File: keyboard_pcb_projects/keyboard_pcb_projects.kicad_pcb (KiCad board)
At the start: 2 copper layers, 157 parts, among them J1 AVR-ISP-6, SW1 SW_Push_Reset, SW10 8, SW11 9, SW12 0, SW13 -, SW14 =, SW15 Backspace, SW16 Page Up, SW17 Tab, SW18 Q, SW19 W, SW20 E, SW21 R, SW22 T, SW23 Y, SW24 U, SW25 I, SW26 O, SW27 P, SW28 [, SW29 ], SW3 1, SW30 \, SW31 Page Dn, SW32 Caps Lock, SW33 A, SW34 S, SW35 D, SW36 F, SW37 G, SW38 H, SW39 J, SW4 2, SW40 K, SW41 L, SW42 ;, SW43 ', SW44 Enter, SW46 Insert, SW47 Shift Left, SW48 Z, SW49 X, SW5 3, SW50 C, SW51 V, SW52 B, SW53 N, SW54 M, SW55 ,, SW56 ., SW57 /, SW58 Shift Right, SW6 4, SW60 Up, SW61 Delete, SW62 Ctrl, SW63 Win, SW64 Alt, SW65 Space, SW66 Alt, SW67 Fn, SW68 Left, SW69 Down, SW7 5, SW70 Right, SW71 Ctrl, SW8 6, SW9 7, U1 ATmega32U4-A, Y1 Crystal_GND24_Small

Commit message: More wiring progress
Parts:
- moved D1 4.88 mm to (194.1, 79.2)
- moved C2 3.96 mm to (234.2, 177.0)
- moved C3 3.87 mm to (234.2, 174.0)
- moved C4 3.31 mm to (227.2, 169.0)
- moved F1 2.61 mm to (189.0, 83.0)
- moved Y1 2.43 mm to (228.7, 175.4), turned to 90 degrees
- moved R6 1.18 mm to (199.0, 76.0)
- moved R5 1.06 mm to (189.0, 76.0)
- moved C1 1.03 mm to (218.5, 166.5)
- moved USB1 0.47 mm to (194.0, 63.7)
- turned C6 to 90 degrees
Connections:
- C5 pad 1: Net-(C5-Pad1) -> +5V
- C6 pad 1: Net-(C5-Pad1) -> +5V
- C7 pad 1: Net-(C5-Pad1) -> +5V
- C8 pad 1: Net-(C5-Pad1) -> +5V
- R5 pad 1: Net-(USB1-CC2) -> Net-(USB1-CC1)
- R6 pad 1: Net-(USB1-CC1) -> Net-(USB1-CC2)
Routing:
- net row4: track 0.00 -> 288.1 mm
- net row0: track 0.00 -> 285.8 mm
- net row1: track 0.00 -> 281.0 mm
- net row2: track 0.00 -> 278.6 mm
- net row3: track 0.00 -> 273.8 mm
- net GND: track 0.00 -> 220.0 mm, vias 0 -> 9
- net +5V: track 0.00 -> 204.8 mm, vias 0 -> 7
- net /USB_D_N: track 0.00 -> 104.9 mm, vias 0 -> 2
- net /USB_D_P: track 5.45 -> 108.1 mm, vias 0 -> 2
- net col14: track 0.00 -> 77.7 mm, vias 0 -> 5
- net VCC: track 0.00 -> 24.8 mm, vias 0 -> 2
- net Net-(D71-A): track 0.00 -> 16.0 mm
- net Net-(D69-A): track 0.00 -> 16.0 mm
- net Net-(D68-A): track 0.00 -> 16.0 mm
- net Net-(D66-A): track 0.00 -> 16.0 mm
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- added copper zone on B.Cu, net GND
- added copper zone on F.Cu, net GND
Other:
- board outline added: 332 x 137.5 mm

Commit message: synchronizing between OS workspaces
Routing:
- net col0: track 85.6 -> 258.6 mm, vias 5 -> 9
- net col14: track 77.7 -> 232.6 mm, vias 5 -> 7
- net col1: track 95.4 -> 244.9 mm, vias 5 -> 9
- net col13: track 80.7 -> 216.3 mm, vias 4 -> 8
- net col2: track 93.1 -> 219.6 mm, vias 5 -> 9
- net col12: track 90.0 -> 203.6 mm, vias 4 -> 8
- net row1: track 281.0 -> 384.9 mm, vias 0 -> 2
- net col3: track 91.0 -> 190.7 mm, vias 5 -> 9
- net col4: track 67.0 -> 156.5 mm, vias 4 -> 10
- net row0: track 285.8 -> 373.3 mm, vias 0 -> 9
- net +5V: track 204.8 -> 285.3 mm, vias 7 -> 6
- net col11: track 97.4 -> 175.8 mm, vias 5 -> 6
- net RESET: track 0.00 -> 73.3 mm, vias 0 -> 7
- net col9: track 67.0 -> 133.1 mm, vias 4 -> 8
- net col10: track 88.5 -> 151.2 mm, vias 5 -> 8
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
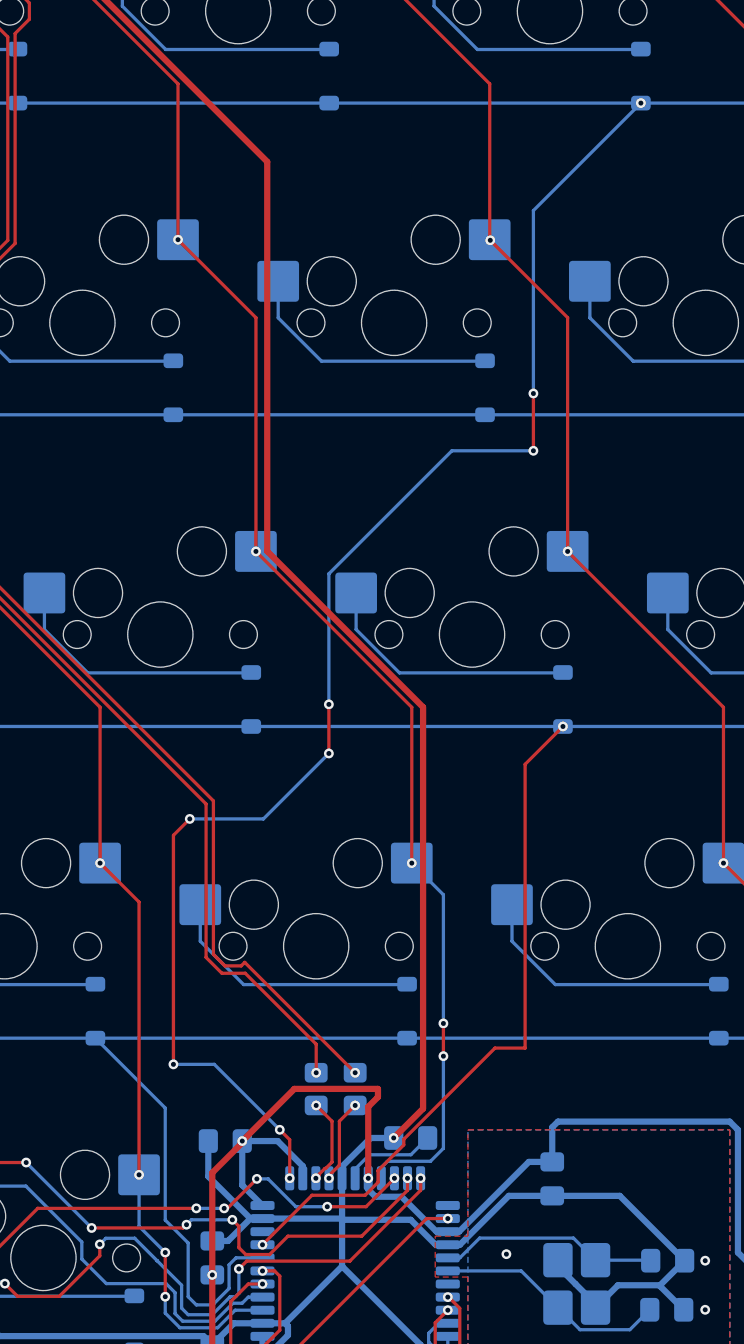
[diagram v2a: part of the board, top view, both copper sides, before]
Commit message: finally cleared all errors but the inherent usbc port sizing issue
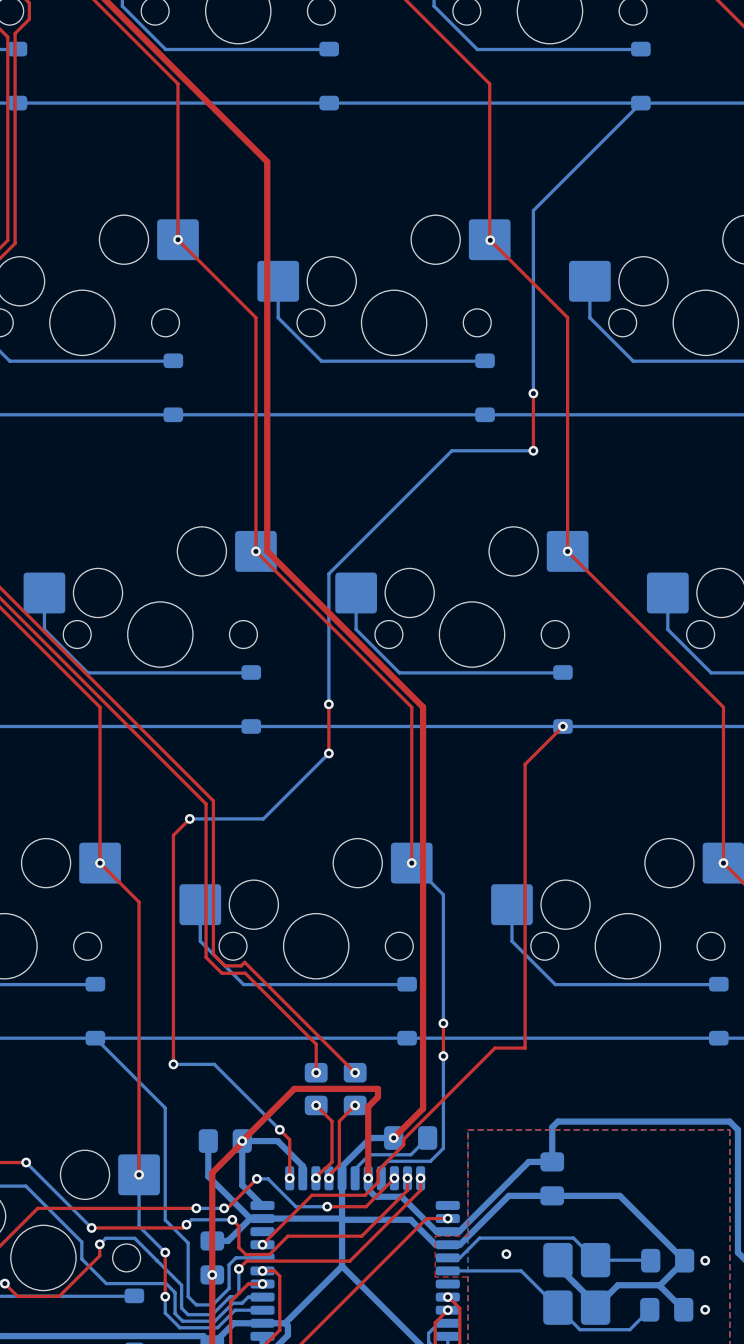
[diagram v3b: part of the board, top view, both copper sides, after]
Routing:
- net row0: vias 9 -> 8
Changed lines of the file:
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@@
 		(tags "capacitor handsolder")
 		(property "Reference" "C5"
-			(at 0 1.68 90)
+			(at 4.33125 -1.375 90)
 			(layer "B.SilkS")
 			(effects
@@
 		(tags "resistor handsolder")
 		(property "Reference" "R4"
-			(at 0 1.65 90)
+			(at -2.0125 4.60625 180)
 			(layer "B.SilkS")
 			(effects
@@
 		(tags "capacitor handsolder")
 		(property "Reference" "C3"
-			(at 0 1.68 0)
+			(at 2.79375 1.68 0)
 			(layer "B.SilkS")
 			(effects
@@
 		(tags "TQFP QFP Microchip_44-Lead-Plastic-Thin-Quad-Flatpack-(PT)")
 		(property "Reference" "U1"
-			(at 0 7.35 90)
+			(at 0.375 3.60625 90)
 			(layer "B.SilkS")
 			(effects
@@
 	(segment
 		(start 201.633679 172.63035)
-		(end 201.63035 172.63035)
+		(end 199.86965 172.63035)
 		(width 0.2)
 		(layer "B.Cu")
@@
 	)
 	(segment
-		(start 207.46863 176.2)
-		(end 206.368628 177.3)
+		(start 203.003329 174)
+		(end 203 174)
 		(width 0.2)
 		(layer "B.Cu")
@@
 	)
 	(segment
-		(start 206.368628 177.3)
-		(end 204.9 177.3)
+		(start 204.5 176.9)
+		(end 204.5 175.496671)
 		(width 0.2)
 		(layer "B.Cu")
@@
 	)
 	(segment
-		(start 208 176.000001)
-		(end 207.800001 176.2)
+		(start 208 174.5)
+		(end 208 176.000001)
 		(width 0.2)
 		(layer "B.Cu")
@@
 	)
 	(segment
-		(start 207.800001 176.2)
-		(end 207.46863 176.2)
+		(start 193.6 175.3)
+		(end 191.7 175.3)
 		(width 0.2)
 		(layer "B.Cu")
@@
 	)
 	(segment
-		(start 204.5 175.496671)
-		(end 203.003329 174)
+		(start 207.46863 176.2)
+		(end 206.368628 177.3)
 		(width 0.2)
 		(layer "B.Cu")
@@
 	)
 	(segment
-		(start 199.5 173)
-		(end 199.86965 172.63035)
+		(start 193.7 175.4)
+		(end 193.6 175.3)
 		(width 0.2)
 		(layer "B.Cu")
@@
 	)
 	(segment
-		(start 193.6 175.3)
-		(end 191.7 175.3)
-		(width 0.2)
-		(layer "B.Cu")
-		(net "MISO")
-	)
-	(segment
 		(start 203 173.996671)
 		(end 201.633679 172.63035)
@@
 	)
 	(segment
-		(start 193.7 175.4)
-		(end 193.6 175.3)
+		(start 208 176.000001)
+		(end 207.800001 176.2)
 		(width 0.2)
 		(layer "B.Cu")
@@
 	)
 	(segment
-		(start 204.5 176.9)
-		(end 204.5 175.496671)
+		(start 204.5 175.496671)
+		(end 203.003329 174)
 		(width 0.2)
 		(layer "B.Cu")
@@
 	)
 	(segment
-		(start 208 174.5)
-		(end 208 176.000001)
+		(start 207.800001 176.2)
+		(end 207.46863 176.2)
 		(width 0.2)
 		(layer "B.Cu")
@@
 	(segment
 		(start 199.86965 172.63035)
-		(end 201.633679 172.63035)
+		(end 199.5 173)
 		(width 0.2)
 		(layer "B.Cu")
@@
 	)
 	(segment
-		(start 203.003329 174)
-		(end 203 174)
+		(start 206.368628 177.3)
+		(end 204.9 177.3)
 		(width 0.2)
 		(layer "B.Cu")
@@
 		(size 0.6)
 		(drill 0.3)
-		(layers "F.Cu" "B.Cu")
-		(net "row0")
-	)
-	(via
-		(at 232.56875 103.25)
-		(size 0.6)
-		(drill 0.3)
